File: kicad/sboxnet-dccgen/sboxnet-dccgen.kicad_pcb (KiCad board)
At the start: 2 copper layers, 28 x 47 mm, 12 parts, among them J1 sboxnet-stecker_02x17, J2 Screw_Terminal_01x02, U1 SN65HVD230

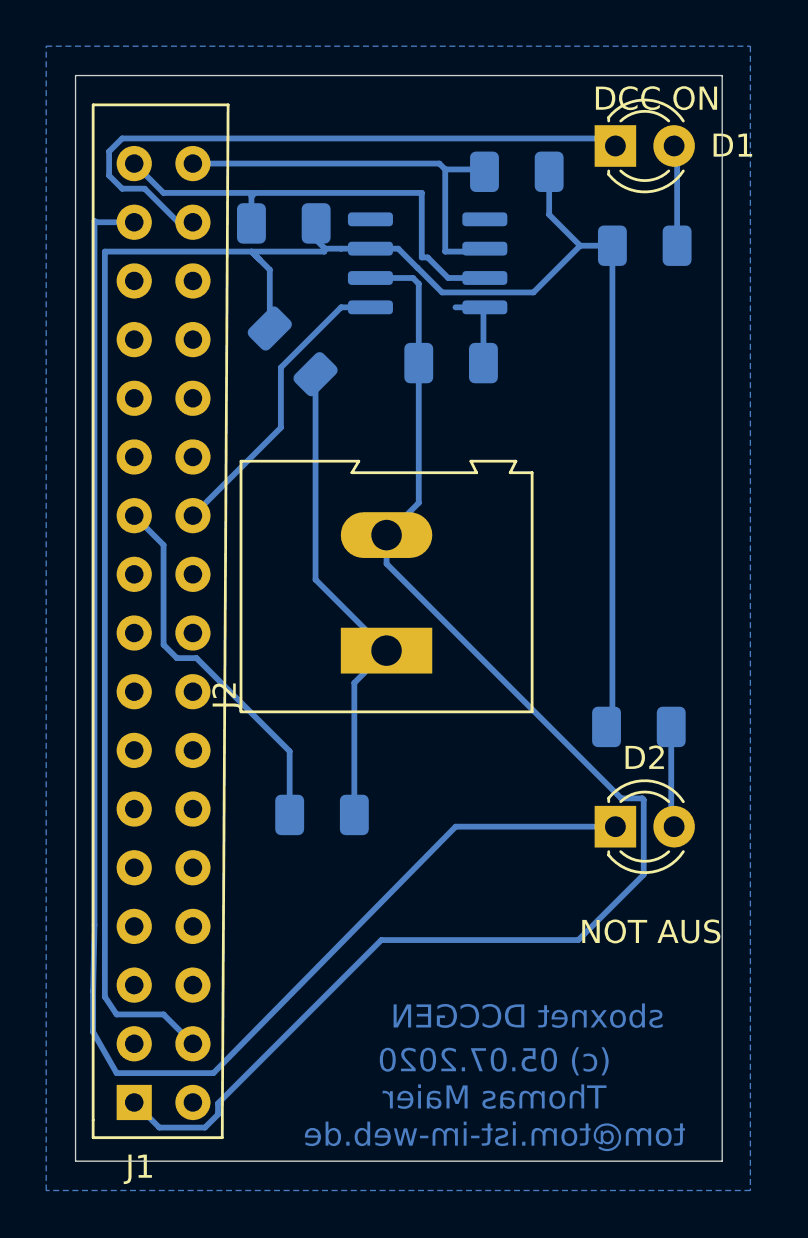
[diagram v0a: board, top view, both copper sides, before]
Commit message: booster DCC Input
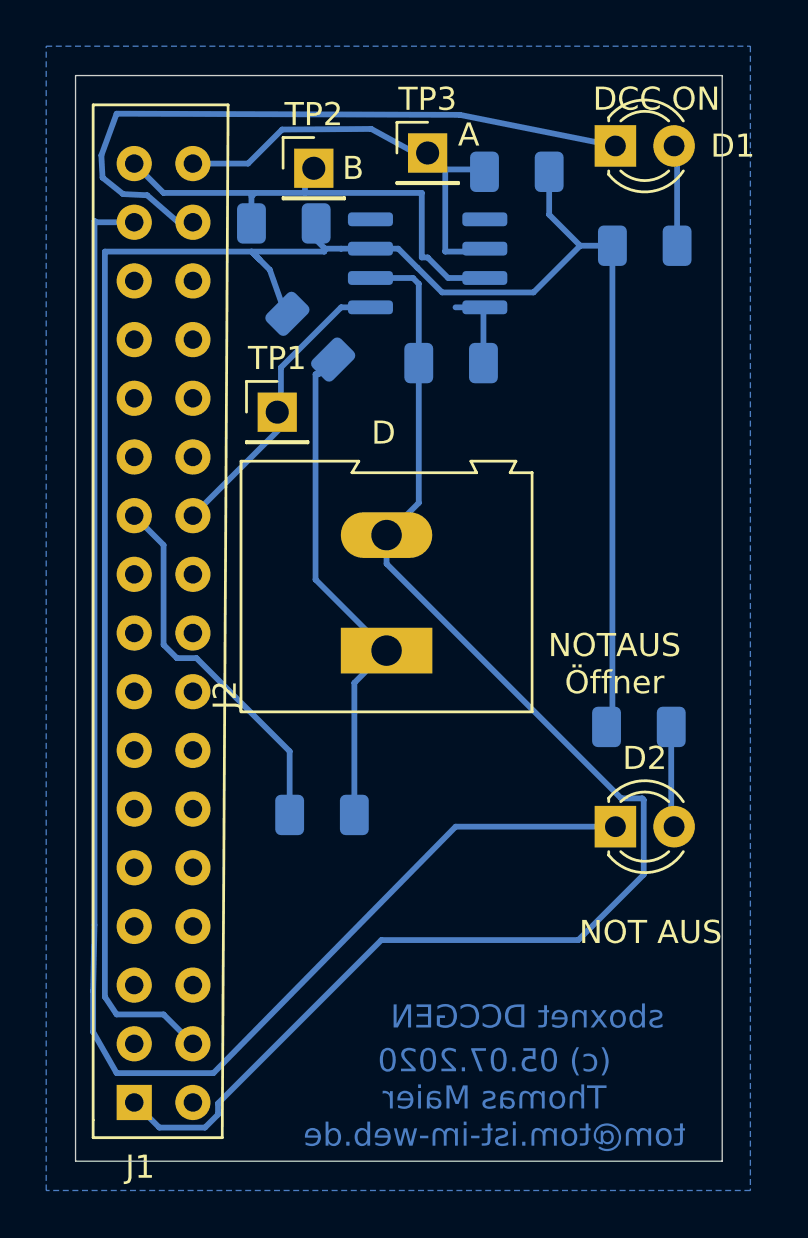
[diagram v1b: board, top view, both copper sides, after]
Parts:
- added TP1: TestPoint, Connector_PinHeader_2.54mm:PinHeader_1x01_P2.54mm_Vertical, F.Cu at (35.4, 64.1)
- added TP2: TestPoint, Connector_PinHeader_2.54mm:PinHeader_1x01_P2.54mm_Vertical, F.Cu at (37.0, 53.5)
- added TP3: TestPoint, Connector_PinHeader_2.54mm:PinHeader_1x01_P2.54mm_Vertical, F.Cu at (41.9, 52.9)
- moved R3 0.99 mm to (36.8, 60.8)
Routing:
- net PD6: track 27.8 -> 29.2 mm
- net DCC_B: track 20.2 -> 21.4 mm
- net Net-(J2-Pad1): track 20.9 -> 22.0 mm
- net DCC_A: track 18.1 -> 19.0 mm
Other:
- board text added: "A"
- board text added: "B"
- board text added: "D"
- board text added: "NOTAUS Öffner"
